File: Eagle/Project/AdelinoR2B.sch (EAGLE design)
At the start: 70 parts, among them J1 DC-044-A, J2 YELLOW-8P-2.54, J3 YELLOW-6P-2.54, J4 YELLOW-8P-2.54, J5 YELLOW-8P-2.54, J6 4P-2.0, J7 YELLOW-2X3P-2.54, J8 4P-2.0, Q1 NCE3407A, Q2 CJ2305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

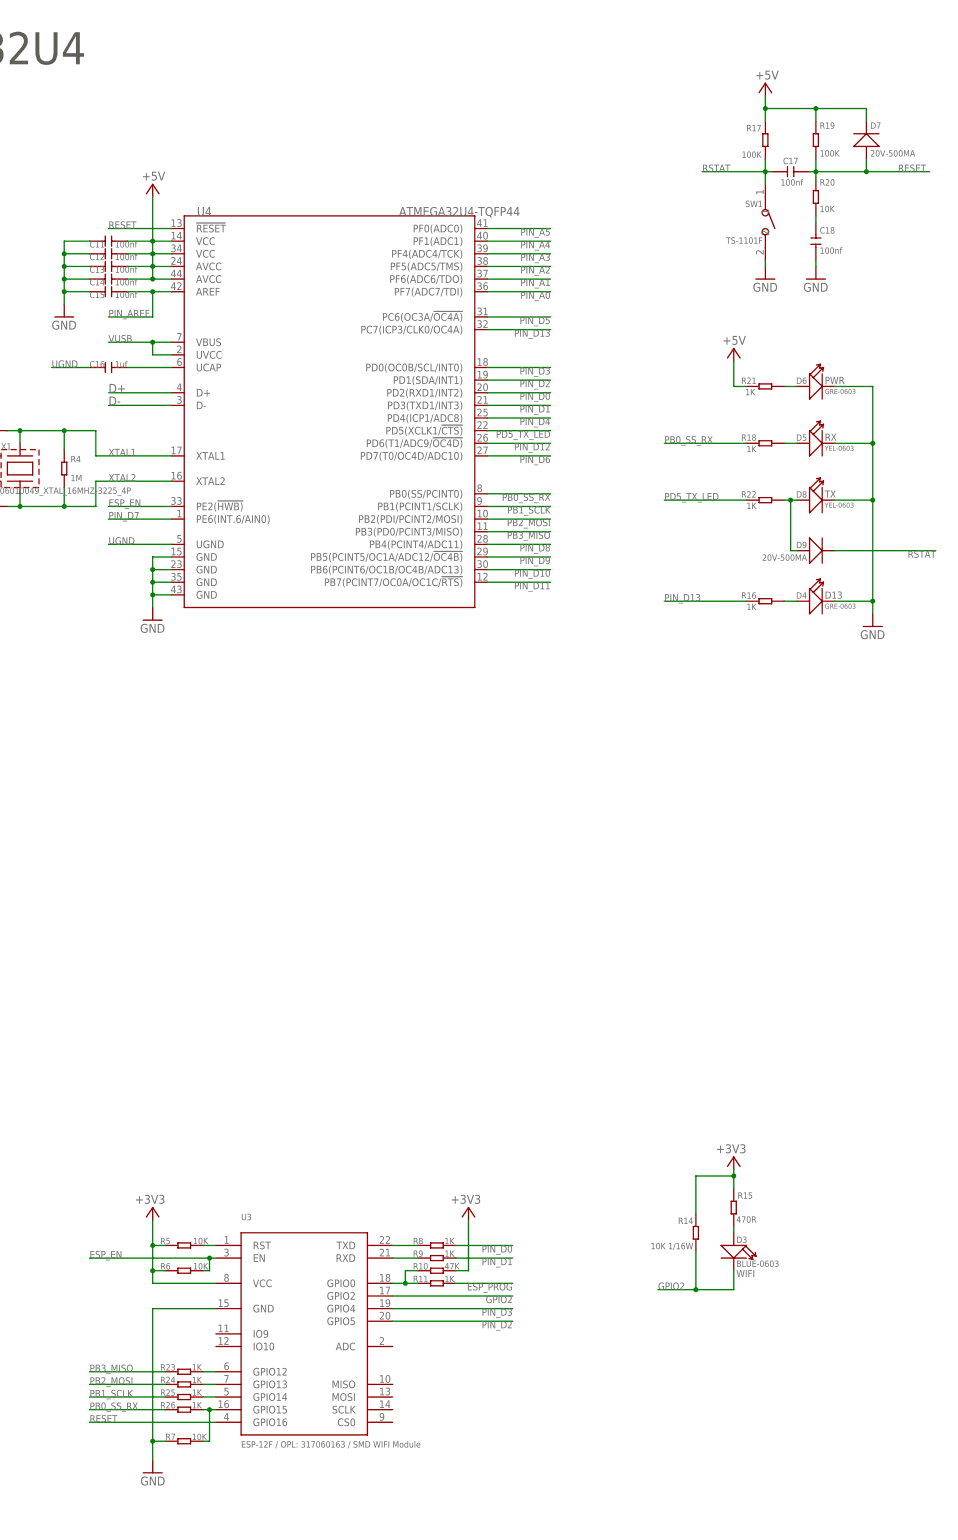
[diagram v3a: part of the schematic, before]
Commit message: ATmega/Esp control pins reviewed.
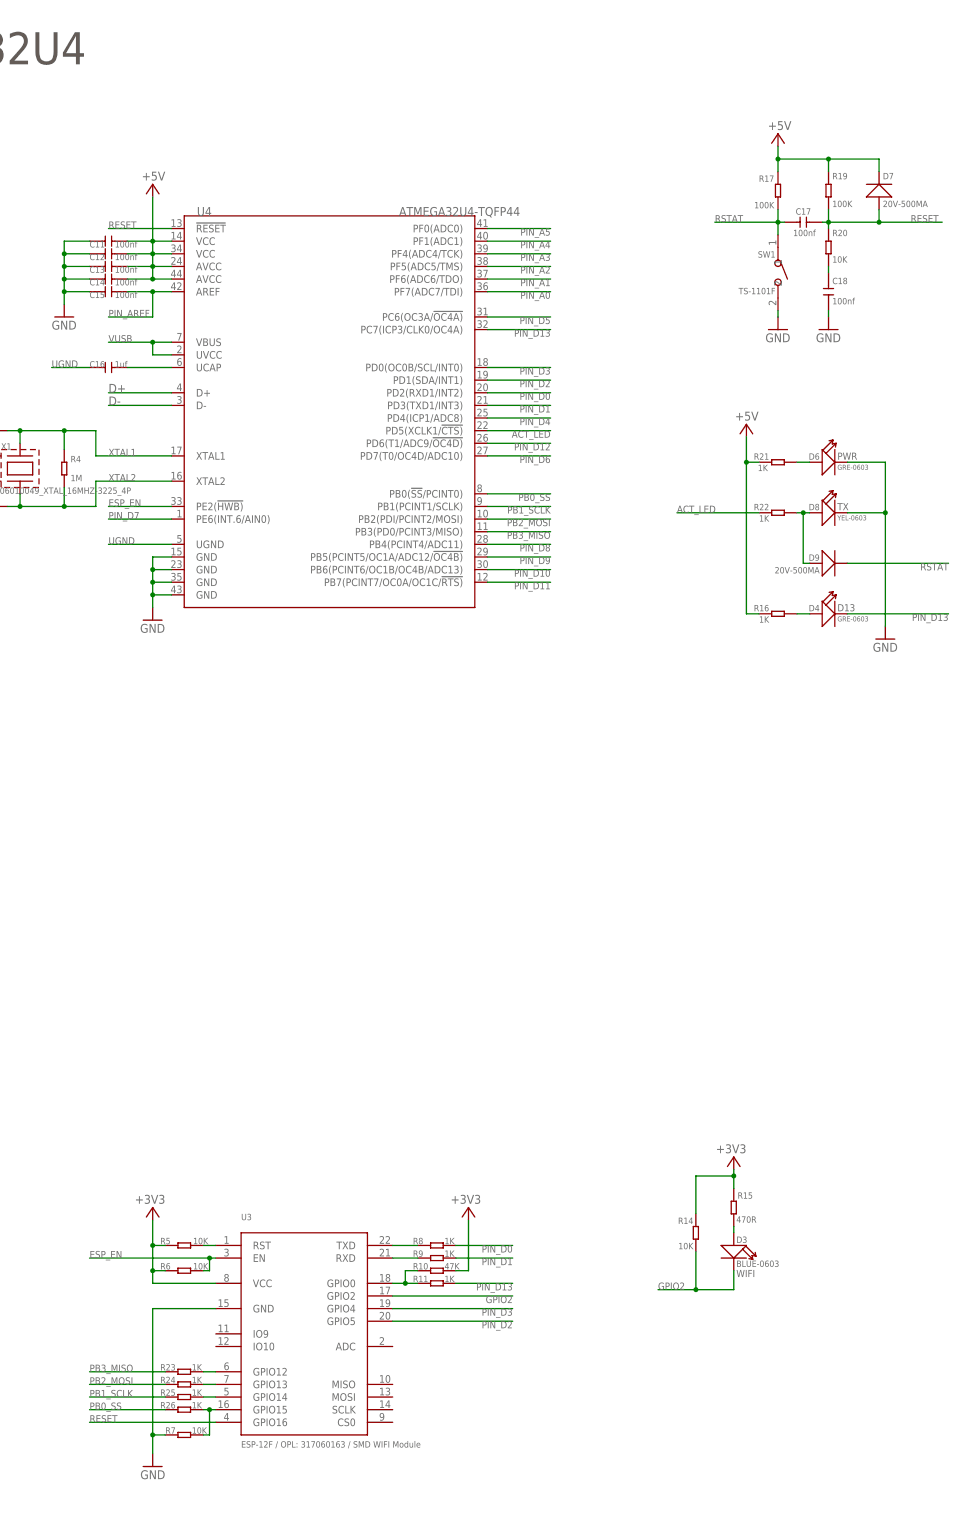
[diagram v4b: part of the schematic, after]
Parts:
- removed D5: YEL-0603, Seeed-LED:SMD-LED-CLEAR-YELLOW(0603)
- removed R18: 1K, Seeed-Resistor:SMD-RES-1K-5%-1/16W(0402)
- R14: value 10K 1/16W -> 10K
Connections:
- net PD5_TX_LED renamed ACT_LED
- removed net ESP_PROG: R11.2
- removed net N$15: D5.+, R18.2
- removed net PB0_SS_RX: R18.1, R26.1, U4.PB0(SS/PCINT0)
- new net PB0_SS: R26.1, U4.PB0(!SS!/PCINT0)
- net +5V: now also R16.1
- net GND: no longer D4.-, D5.-
- net PIN_D13: now also D4.-, R11.2; no longer R16.1
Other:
- moved on the sheet: C17, C18, D4, D6, D7, D8, D9, R16, R17, R19, R20, R21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

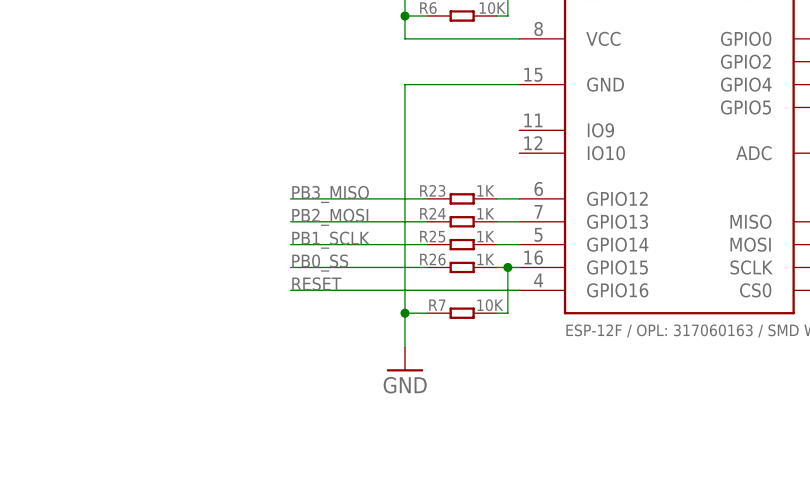
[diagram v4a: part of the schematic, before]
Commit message: Reserve resistor for GPIO16/RESET.
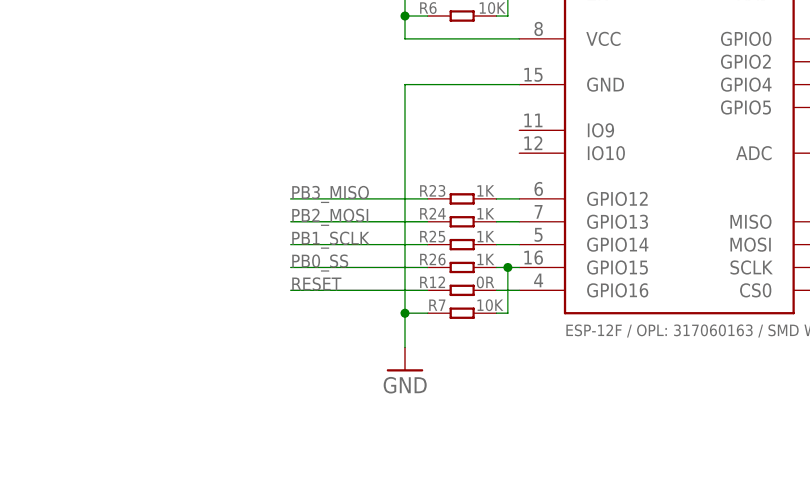
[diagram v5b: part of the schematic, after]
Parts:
- added R12: 0R, Seeed-Resistor:SMD-RES-0R-5%-1/16W(0402)
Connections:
- new net N$11: R12.2, U3.GPIO16
- net RESET: now also R12.1; no longer U3.GPIO16
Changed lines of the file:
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@@
 <part name="R25" library="Seeed-Resistor" deviceset="SMD-RES-1K-5%-1/16W(0402)" device="" value="1K"/>
 <part name="R26" library="Seeed-Resistor" deviceset="SMD-RES-1K-5%-1/16W(0402)" device="" value="1K"/>
+<part name="R12" library="Seeed-Resistor" deviceset="SMD-RES-0R-5%-1/16W(0402)" device="" value="0R"/>
 </parts>
 <sheets>
@@
 <attribute name="NAME" x="82.804" y="-103.886" size="1.27" layer="95" ratio="10"/>
 <attribute name="VALUE" x="89.154" y="-103.886" size="1.27" layer="96" ratio="10"/>
+</instance>
+<instance part="R12" gate="G$1" x="87.63" y="-106.68" smashed="yes">
+<attribute name="NAME" x="82.804" y="-106.426" size="1.27" layer="95" ratio="10"/>
+<attribute name="VALUE" x="89.154" y="-106.426" size="1.27" layer="96" ratio="10"/>
 </instance>
 </instances>
@@
 </segment>
 <segment>
-<pinref part="U3" gate="G$1" pin="GPIO16"/>
-<wire x1="93.98" y1="-106.68" x2="68.58" y2="-106.68" width="0.1524" layer="91"/>
 <label x="68.58" y="-106.68" size="1.4224" layer="95"/>
+<wire x1="83.82" y1="-106.68" x2="68.58" y2="-106.68" width="0.1524" layer="91"/>
+<pinref part="R12" gate="G$1" pin="1"/>
 </segment>
 </net>
@@
 </segment>
 </net>
+<net name="N$11" class="0">
+<segment>
+<pinref part="U3" gate="G$1" pin="GPIO16"/>
+<wire x1="93.98" y1="-106.68" x2="91.44" y2="-106.68" width="0.1524" layer="91"/>
+<pinref part="R12" gate="G$1" pin="2"/>
+</segment>
+</net>

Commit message: Wip.
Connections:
- net +5V: no longer R16.1
- net GND: now also D4.-
- net PIN_D13: now also R16.1; no longer D4.-
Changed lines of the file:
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@@
 <wire x1="220.98" y1="86.36" x2="228.6" y2="86.36" width="0.1524" layer="91"/>
 <wire x1="228.6" y1="86.36" x2="228.6" y2="76.2" width="0.1524" layer="91"/>
-<wire x1="228.6" y1="76.2" x2="228.6" y2="53.34" width="0.1524" layer="91"/>
+<wire x1="228.6" y1="76.2" x2="228.6" y2="55.88" width="0.1524" layer="91"/>
 <pinref part="D8" gate="G$1" pin="-"/>
+<wire x1="228.6" y1="55.88" x2="228.6" y2="53.34" width="0.1524" layer="91"/>
 <wire x1="220.98" y1="76.2" x2="228.6" y2="76.2" width="0.1524" layer="91"/>
 <junction x="228.6" y="76.2"/>
+<pinref part="D4" gate="G$1" pin="-"/>
+<wire x1="220.98" y1="55.88" x2="228.6" y2="55.88" width="0.1524" layer="91"/>
+<junction x="228.6" y="55.88"/>
 </segment>
 </net>
@@
 <wire x1="200.66" y1="91.44" x2="200.66" y2="86.36" width="0.1524" layer="91"/>
 <wire x1="200.66" y1="86.36" x2="203.2" y2="86.36" width="0.1524" layer="91"/>
-<pinref part="R16" gate="G$1" pin="1"/>
-<wire x1="203.2" y1="55.88" x2="200.66" y2="55.88" width="0.1524" layer="91"/>
-<wire x1="200.66" y1="55.88" x2="200.66" y2="86.36" width="0.1524" layer="91"/>
-<junction x="200.66" y="86.36"/>
 </segment>
 </net>
@@
 </segment>
 <segment>
-<pinref part="D4" gate="G$1" pin="-"/>
-<wire x1="220.98" y1="55.88" x2="241.3" y2="55.88" width="0.1524" layer="91"/>
-<label x="241.3" y="55.88" size="1.4224" layer="95" rot="R180"/>
-</segment>
-</net>
+<pinref part="R16" gate="G$1" pin="1"/>
+<wire x1="203.2" y1="55.88" x2="186.69" y2="55.88" width="0.1524" layer="91"/>
+<label x="186.69" y="55.88" size="1.4224" layer="95"/>
+</segment>
+</net>
